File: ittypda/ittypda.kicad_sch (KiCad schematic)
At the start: 135 parts, among them J1 USB_C_Receptacle_USB2.0_14P, SW1 SW_SPDT, U1 STM32F401RETx, Y1 16Mhz

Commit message: reorganize schem
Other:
- note added: "USB-C"
- moved on the sheet: C1, C10, C2, C3, C4, C5, C6, C7, C8, C9, J1, R1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

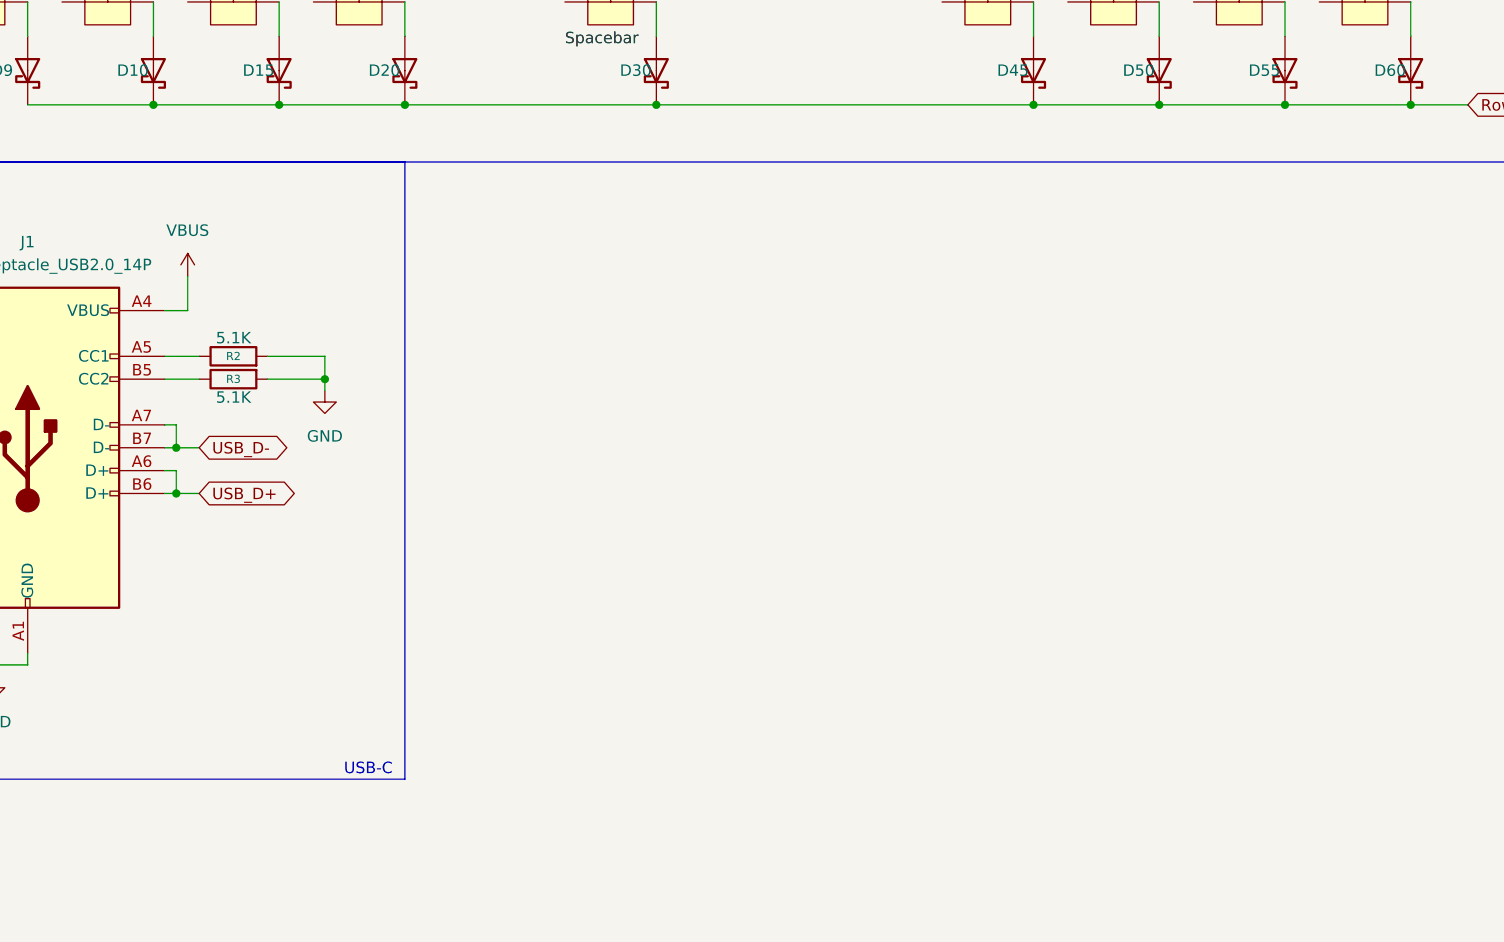
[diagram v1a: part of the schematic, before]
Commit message: add BQ24040 charging IC
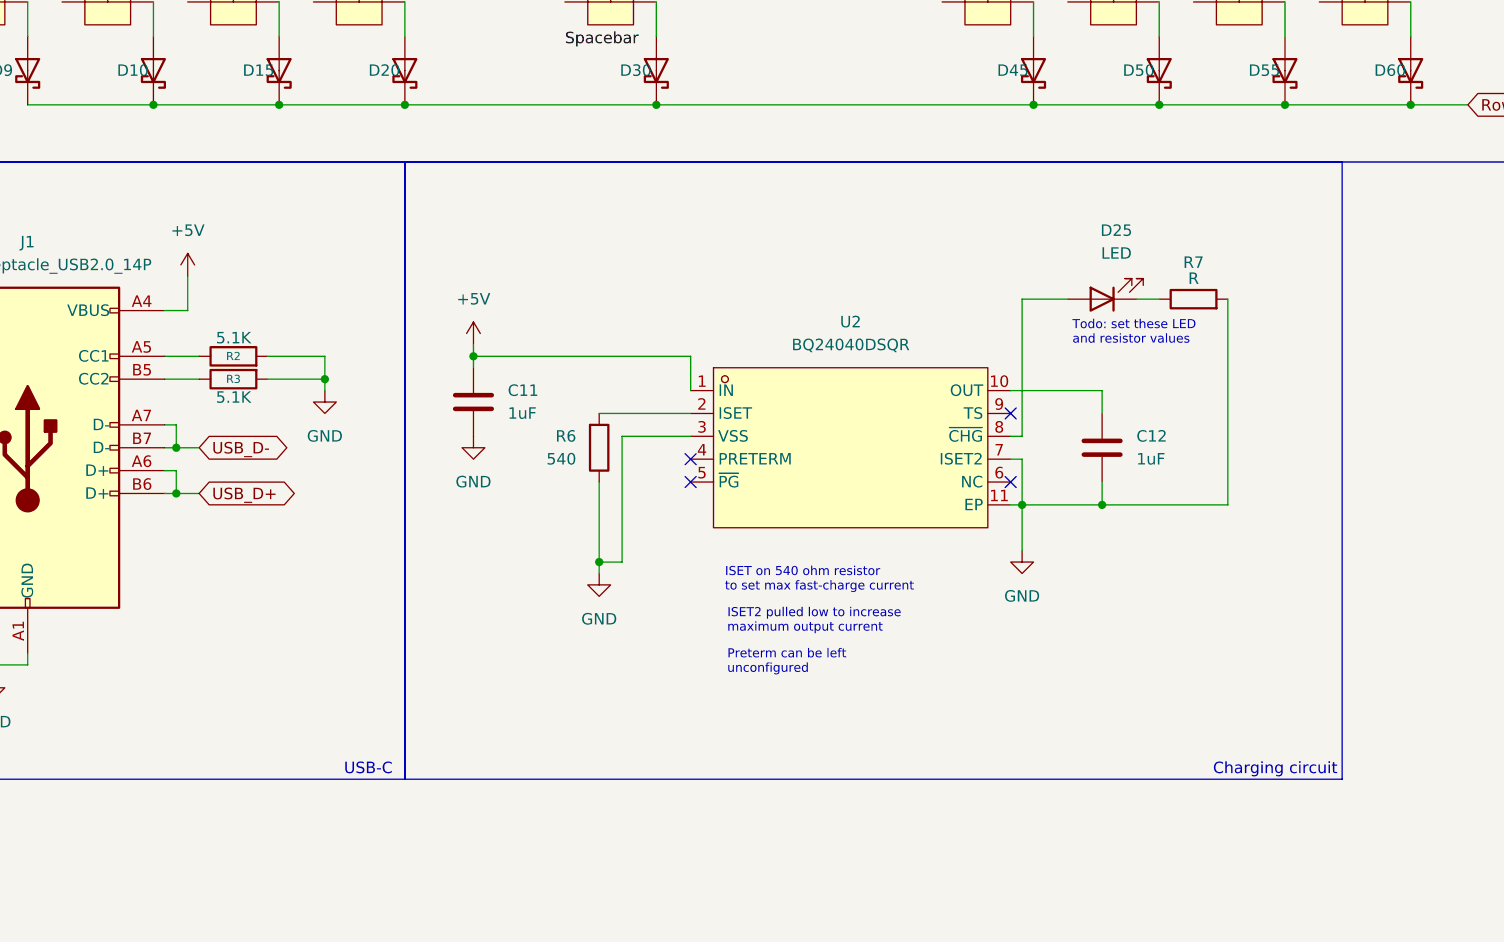
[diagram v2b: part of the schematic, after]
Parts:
- added C11, C12: 1uF, symbol Device:C
- added D25: LED, symbol Device:LED
- added R6: 540, symbol Device:R
- added R7: R, symbol Device:R
- added U2: BQ24040DSQR, easyeda2kicad:WSON-10_L2.0-W2.0-P0.40-BL-EP, symbol easyeda2kicad:BQ24040DSQR
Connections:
- net GND: now also C11.2, C12.2, R6.1, R7.2, U2.11 (EP), U2.3 (VSS), U2.7 (ISET2)
- net VBUS renamed +5V
- net +5V: now also C11.1, U2.1 (IN)
- new net: D25.1 (K), R7.1
- new net: D25.2 (A), U2.8 (~{CHG})
- new net: C12.1, U2.10 (OUT)
- new net: R6.2, U2.2 (ISET)
- no-connect marks 4 -> 8
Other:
- note added: "Charging circuit"
- note added: "ISET on 540 ohm resistor to set max fast-charge current"
- note added: "ISET2 pulled low to increase maximum output current"
- note added: "Preterm can be left unconfigured"
- note added: "Todo: set these LED and resistor values"

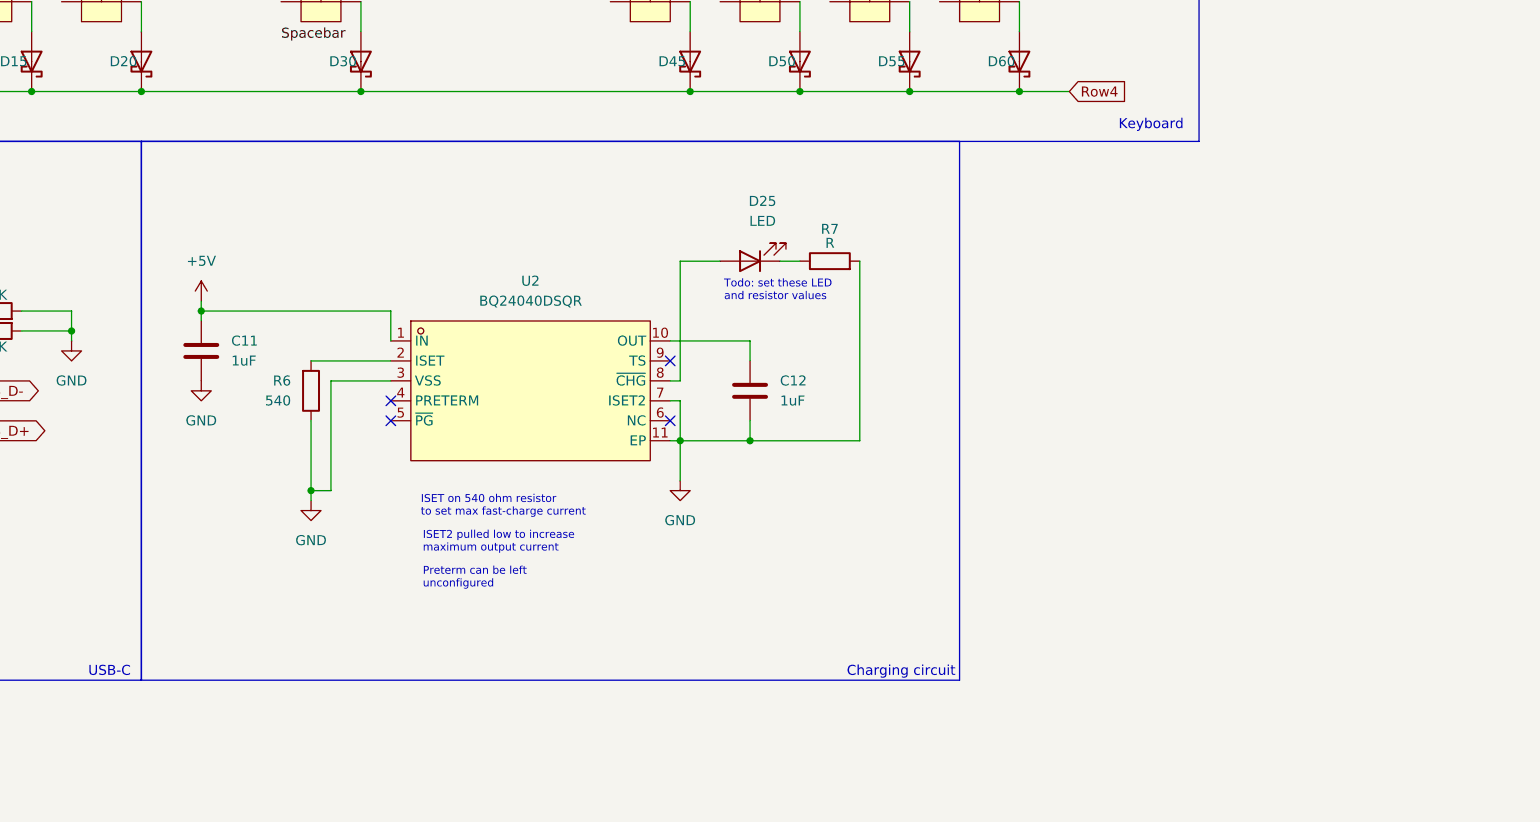
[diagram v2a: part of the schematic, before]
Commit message: add linear regulator.. we have power!!!
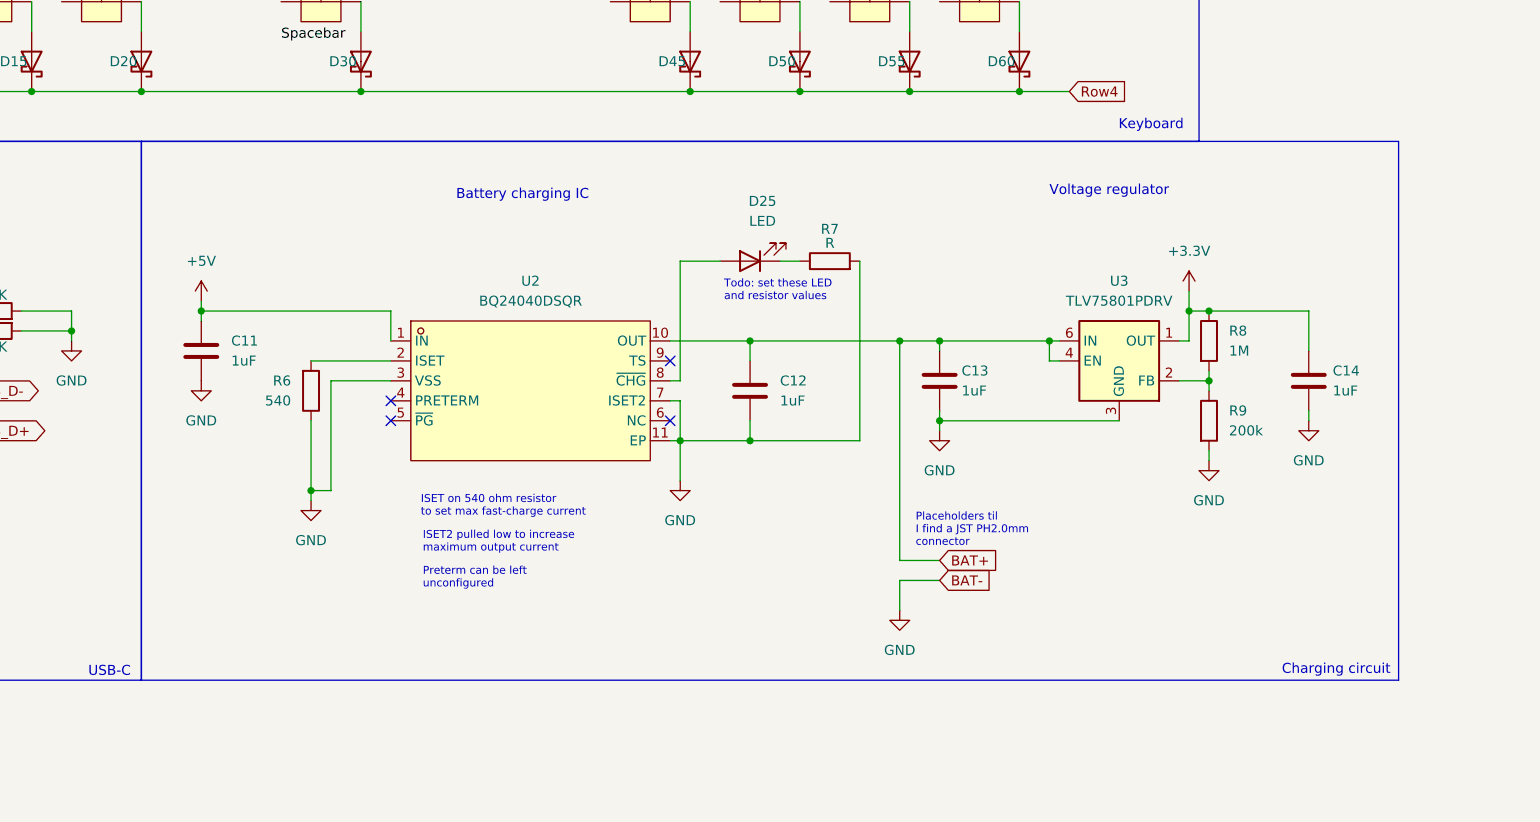
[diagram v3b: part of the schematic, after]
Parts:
- added C13, C14: 1uF, symbol Device:C
- added R8: 1M, symbol Device:R
- added R9: 200k, symbol Device:R
- added U3: TLV75801PDRV, Package_SON:WSON-6-1EP_2x2mm_P0.65mm_EP1x1.6mm, symbol Regulator_Linear:TLV75801PDRV
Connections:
- net +3.3V: now also C14.1, R8.1, U3.1 (OUT)
- net GND: now also C13.2, C14.2, R9.2, U3.3 (GND), U3.7 (GND)
- net BAT+: now reaches C12.1, U2.10 (OUT)
- net BAT+: now also C13.1, U3.4 (EN), U3.6 (IN)
- new net: R8.2, R9.1, U3.2 (FB)
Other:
- note added: "Battery charging IC"
- note added: "Placeholders til I find a JST PH2.0mm connector"
- note added: "Voltage regulator"
